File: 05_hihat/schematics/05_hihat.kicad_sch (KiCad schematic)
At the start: 69 parts, among them J1 Output, J2 Gate In, J3 Eurorack 10 pin, J4 Accent CV In, J5 Decay CV, Q1 BC548, Q2 BC548, Q4 BC558, Q5 BC558, U1 TL074, U2 40106

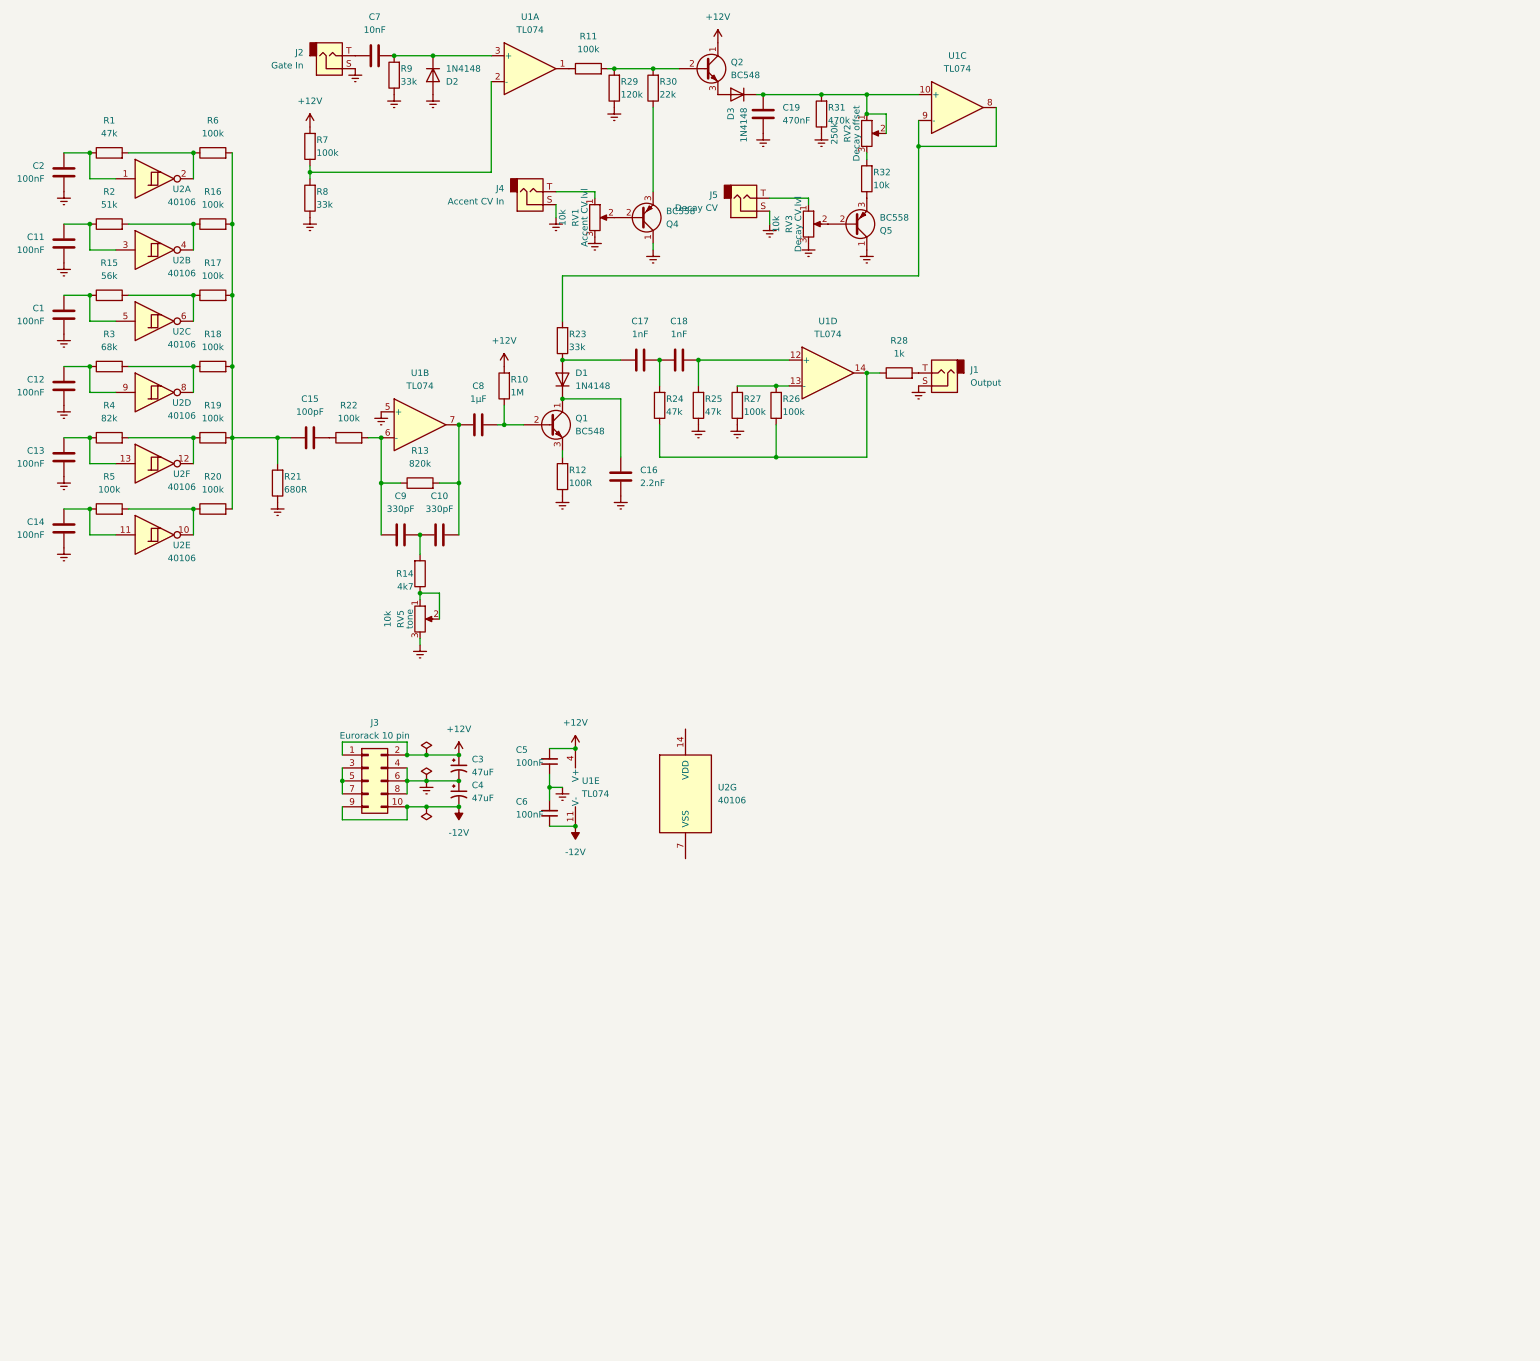
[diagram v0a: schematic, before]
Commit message: added stripboard for 05 hihat
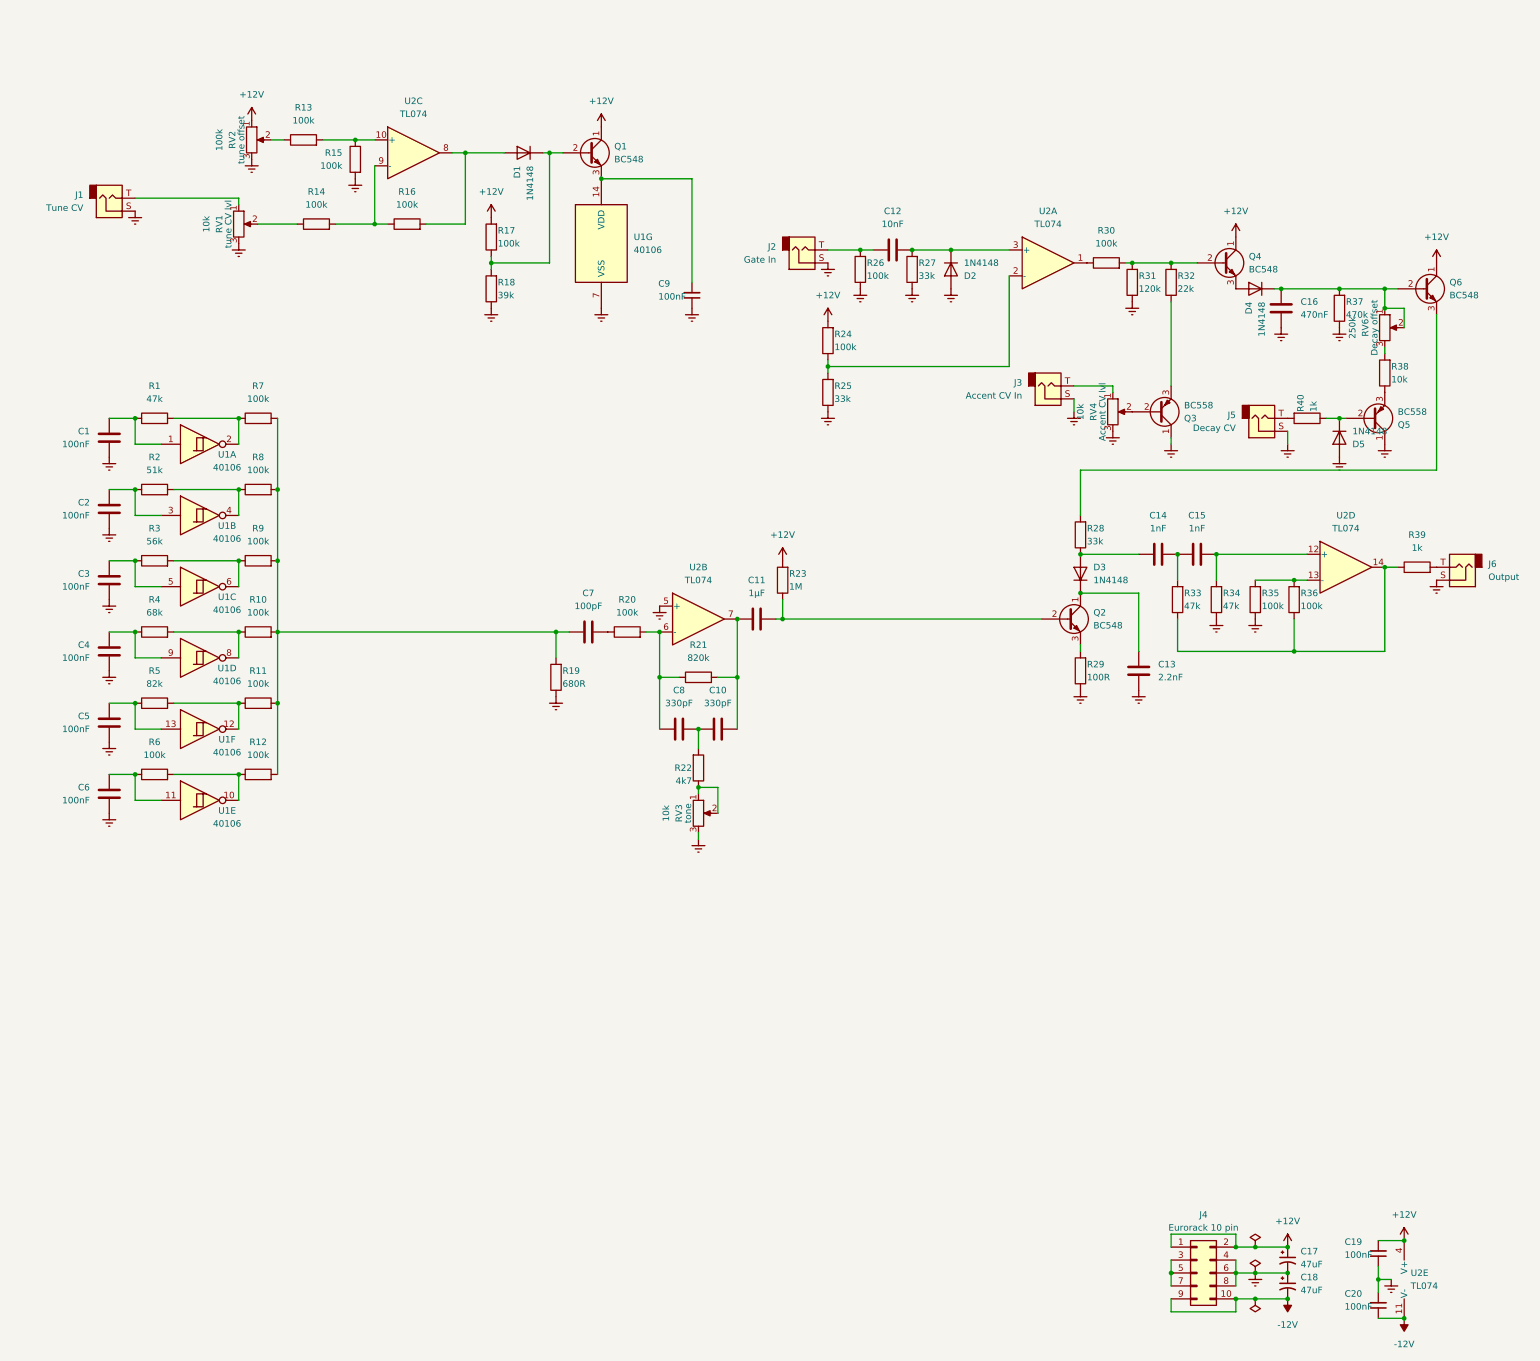
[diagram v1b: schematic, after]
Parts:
- removed C11, C12, C13, C14: 100nF, Capacitor_THT:C_Rect_L7.0mm_W2.5mm_P5.00mm, symbol Device:C
- removed R19, R20: 100k, Resistor_THT:R_Axial_DIN0207_L6.3mm_D2.5mm_P10.16mm_Horizontal, symbol Device:R
- removed RV3: 10k, Potentiometer_THT:Potentiometer_Alpha_RD901F-40-00D_Single_Vertical, symbol Device:R_Potentiometer
- removed unit 3 of U1
- removed unit 6 of U2
- removed unit 5 of U2
- removed unit 4 of U2
- removed unit 2 of U2
- removed unit 1 of U2
- removed unit 3 of U2
- added C3, C4, C5, C6: 100nF, Capacitor_THT:C_Rect_L7.0mm_W2.5mm_P5.00mm, symbol Device:C
- added C9: 100nF, Capacitor_THT:C_Disc_D6.0mm_W2.5mm_P5.00mm, symbol Device:C_Small
- added D1, D5: 1N4148, Diode_THT:D_T-1_P10.16mm_Horizontal, symbol Device:D
- added J1: Tune CV, Connector_Audio:Jack_6.35mm_Neutrik_NJ5FD-V_Vertical, symbol Connector:AudioJack2
- added Q1, Q6: BC548, Package_TO_SOT_THT:TO-92_Inline, symbol Transistor_BJT:BC548
- added R10, R11, R12, R13, R14, R26, R7, R8, R9: 100k, Resistor_THT:R_Axial_DIN0207_L6.3mm_D2.5mm_P10.16mm_Horizontal, symbol Device:R
- added R40: 1k, Resistor_THT:R_Axial_DIN0207_L6.3mm_D2.5mm_P10.16mm_Horizontal, symbol Device:R
- added RV1: 10k, Potentiometer_THT:Potentiometer_Alpha_RD901F-40-00D_Single_Vertical, symbol Device:R_Potentiometer
- added RV2: 100k, Potentiometer_THT:Potentiometer_Alpha_RD901F-40-00D_Single_Vertical, symbol Device:R_Potentiometer
- added unit 2 of U1
- added unit 4 of U1
- added unit 5 of U1
- added unit 1 of U1
- added unit 6 of U1
- added unit 3 of U1
- added unit 3 of U2
- R15: value 56k -> 100k
- R18: value 100k -> 39k
- R3: value 68k -> 56k
- R4: value 82k -> 68k
- R5: value 100k -> 82k
- renumbered C8 to C11, C7 to C12, C16 to C13, C17 to C14, C18 to C15, C19 to C16, C3 to C17, C4 to C18, C5 to C19, C6 to C20, C15 to C7, C9 to C8, D1 to D3, D3 to D4, J4 to J3, J3 to J4, J1 to J6, Q1 to Q2, Q4 to Q3, Q2 to Q4, R21 to R19, R22 to R20, R13 to R21, R14 to R22, R10 to R23, R7 to R24, R8 to R25, R9 to R27, R23 to R28, R12 to R29, R11 to R30, R29 to R31, R30 to R32, R24 to R33, R25 to R34, R27 to R35, R26 to R36, R31 to R37, R32 to R38, R28 to R39, RV5 to RV3, RV1 to RV4, RV2 to RV6, U2 to U1, U1 to U2
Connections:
- net +12V: now also R17.2, Q1.1 (C), Q6.1 (C), RV2.1
- net GNDREF: now also R15.2, R18.1, U1.7 (VSS), C3.2, C4.2, C5.2, C6.2, C9.1, D5.2 (A), J1.S, R26.1, RV1.3, RV2.3
- net at J5.T: now also R40.2
- net at R2.1: now also C2.1, U1.3
- net at R4.2: now also R10.1, U1.8
- net at R4.1: now also C4.1, U1.9
- net at U1.14 (VDD): now also C9.2, Q1.3 (E)
- net at R5.2: now also R11.1, U1.12
- net at R5.1: now also C5.1, U1.13
- net at C12.1, J2.T: now also R26.2
- net at Q5.2 (B): now also D5.1 (K), R40.1
- net at R3.1: now also C3.1, U1.5
- net at R3.2: now also R9.1, U1.6; no longer R18.1
- net at C16.1, D4.1 (K), R37.2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: now also Q6.2 (B)
- net at R1.1: now also C1.1, U1.1; no longer C2.1
- net at R2.2: now also R8.1, U1.4; no longer R16.1
- net at R15.1: now also R13.2, U2.10 (+); no longer C1.1
- net at R17.1: now also R18.2, D1.1 (K), Q1.2 (B); no longer R15.2
- net at R28.2: now also Q6.3 (E)
- net at R6.1: now also C6.1, U1.11; no longer R1.2
- new net: J1.T, RV1.1
- new net: R14.1, RV1.2
- new net: R14.2, R16.1, U2.9 (-)
- new net: D1.2 (A), R16.2, U2.8
- new net: C7.1, R10.2, R11.2, R12.2, R19.2, R7.2, R8.2, R9.2
- new net: R1.2, R7.1, U1.2
- new net: R12.1, R6.2, U1.10
- new net: R13.1, RV2.2
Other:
- moved on the sheet: C10, C11, C12, C13, C14, C15, C16, C17, C18, C19, C20, C7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

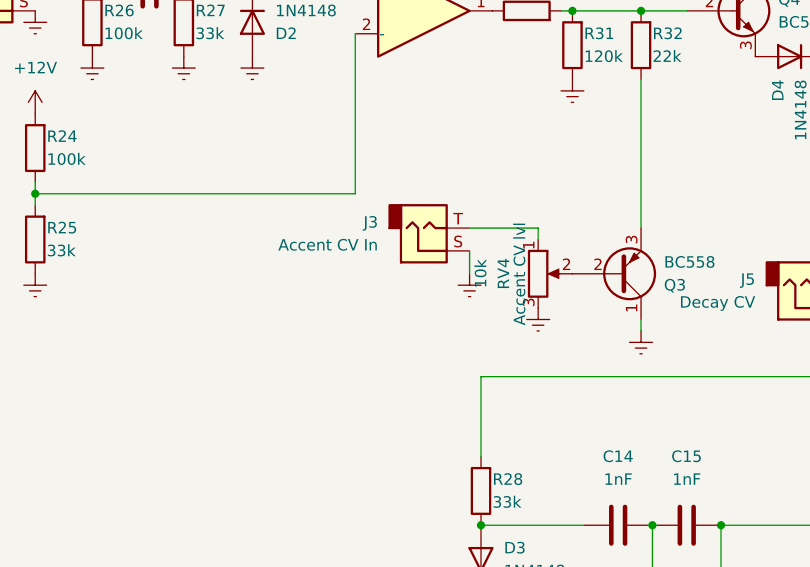
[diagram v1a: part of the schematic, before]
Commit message: fixed some values in the schematic
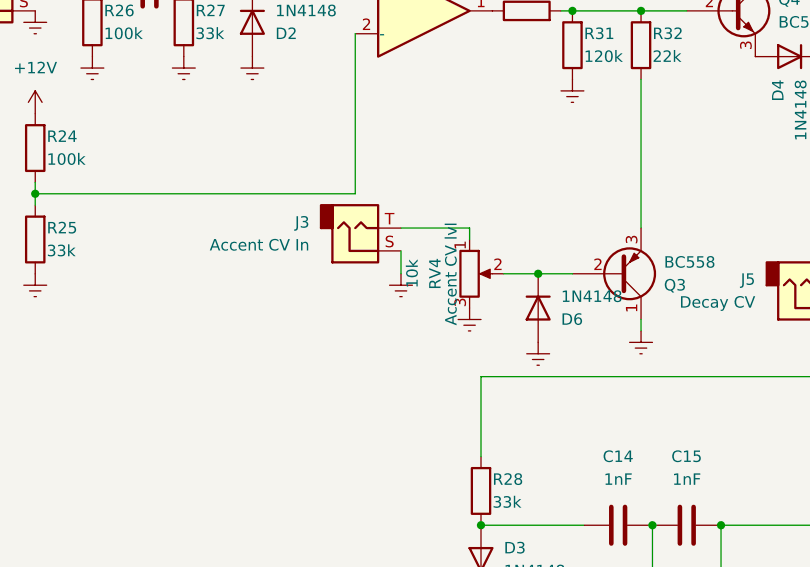
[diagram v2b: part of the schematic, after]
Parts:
- added D6: 1N4148, Diode_THT:D_T-1_P10.16mm_Horizontal, symbol Device:D
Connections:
- net GNDREF: now also D6.2 (A)
- net at Q3.2 (B), RV4.2: now also D6.1 (K)
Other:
- moved on the sheet: J3, RV4
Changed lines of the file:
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@@
 	)
 	(junction
+		(at 229.87 96.52)
+		(diameter 0)
+		(color 0 0 0 0)
+	)
+	(junction
 		(at 58.42 153.67)
 		(diameter 0)
@@
 	(wire
 		(pts
+			(xy 229.87 96.52) (xy 233.68 96.52)
+		)
+		(stroke
+			(width 0)
+			(type default)
+		)
+	)
+	(wire
+		(pts
 			(xy 223.52 116.84) (xy 223.52 107.95)
 		)
@@
 	(wire
 		(pts
+			(xy 226.06 96.52) (xy 229.87 96.52)
+		)
+		(stroke
+			(width 0)
+			(type default)
+		)
+	)
+	(wire
+		(pts
 			(xy 285.75 127) (xy 283.21 127)
 		)
@@
 	(wire
 		(pts
-			(xy 229.87 91.44) (xy 222.25 91.44)
+			(xy 222.25 91.44) (xy 214.63 91.44)
 		)
 		(stroke
@@
 	(wire
 		(pts
-			(xy 229.87 92.71) (xy 229.87 91.44)
+			(xy 222.25 92.71) (xy 222.25 91.44)
 		)
 		(stroke
@@
 	(wire
 		(pts
-			(xy 222.25 96.52) (xy 222.25 93.98)
+			(xy 214.63 96.52) (xy 214.63 93.98)
 		)
 		(stroke
@@
 	(symbol
 		(lib_id "power:GNDREF")
-		(at 222.25 96.52 0)
+		(at 214.63 96.52 0)
 		(unit 1)
 		(exclude_from_sim no)
@@
 		(fields_autoplaced yes)
 		(property "Reference" "#PWR027"
-			(at 222.25 102.87 0)
+			(at 214.63 102.87 0)
 			(effects
 				(font
@@
 		)
 		(property "Value" "GNDREF"
-			(at 222.25 101.6 0)
+			(at 214.63 101.6 0)
 			(effects
 				(font
@@
 		)
 		(property "Footprint" ""
-			(at 222.25 96.52 0)
+			(at 214.63 96.52 0)
 			(effects
 				(font
@@
 		)
 		(property "Datasheet" ""
-			(at 222.25 96.52 0)
+			(at 214.63 96.52 0)
 			(effects
 				(font
@@
 		)
 		(property "Description" ""
-			(at 222.25 96.52 0)
+			(at 214.63 96.52 0)
 			(effects
 				(font
@@
 	(symbol
 		(lib_id "Device:R_Potentiometer")
-		(at 229.87 96.52 0)
+		(at 222.25 96.52 0)
 		(unit 1)
 		(exclude_from_sim no)
@@
 		(dnp no)
 		(property "Reference" "RV4"
-			(at 226.06 96.52 90)
+			(at 218.44 96.52 90)
 			(effects
 				(font
@@
 		)
 		(property "Value" "10k"
-			(at 223.52 96.52 90)
+			(at 215.9 96.52 90)
 			(effects
 				(font
@@
 		)
 		(property "Footprint" "Potentiometer_THT:Potentiometer_Alpha_RD901F-40-00D_Single_Vertical"
-			(at 229.87 96.52 0)
+			(at 222.25 96.52 0)
 			(effects
 				(font
@@
 		)
 		(property "Datasheet" "~"
-			(at 229.87 96.52 0)
+			(at 222.25 96.52 0)
 			(effects
 				(font
@@
 		)
 		(property "Description" "Accent CV lvl"
-			(at 227.838 96.52 90)
+			(at 220.218 96.52 90)
 			(effects
 				(font
@@
 	)
 	(symbol
+		(lib_id "Device:D")
+		(at 229.87 100.33 90)
+		(mirror x)
+		(unit 1)
+		(exclude_from_sim no)
+		(in_bom yes)
+		(on_board yes)
+		(dnp no)
+		(property "Reference" "D6"
+			(at 232.41 101.6001 90)
+			(effects
+				(font
+					(size 1.27 1.27)
+				)
+				(justify right)
+			)
+		)
+		(property "Value" "1N4148"
+			(at 232.41 99.0601 90)
+			(effects
+				(font
+					(size 1.27 1.27)
+				)
+				(justify right)
+			)
+		)
+		(property "Footprint" "Diode_THT:D_T-1_P10.16mm_Horizontal"
+			(at 229.87 100.33 0)
+			(effects
+				(font
+					(size 1.27 1.27)
+				)
+				(hide yes)
+			)
+		)
+		(property "Datasheet" "~"
+			(at 229.87 100.33 0)
+			(effects
+				(font
+					(size 1.27 1.27)
+				)
+				(hide yes)
+			)
+		)
+		(property "Description" ""
+			(at 229.87 100.33 0)
+			(effects
+				(font
+					(size 1.27 1.27)
+				)
+				(hide yes)
+			)
+		)
+		(pin "1"
+		)
+		(pin "2"
+		)
+		(instances
+			(project "05_hihat"
+				(path "/2375ec83-956c-4ce3-8106-f4a8f815549e"
+					(reference "D6")
+					(unit 1)
+				)
+			)
+		)
+	)
+	(symbol
 		(lib_id "Device:C")
 		(at 186.69 64.77 90)
@@
 	(symbol
 		(lib_id "Connector:AudioJack2")
-		(at 217.17 91.44 0)
+		(at 209.55 91.44 0)
 		(mirror x)
 		(unit 1)
@@
 		(dnp no)
 		(property "Reference" "J3"
-			(at 212.09 90.8049 0)
+			(at 204.47 90.8049 0)
 			(effects
 				(font
@@
 		)
 		(property "Value" "Accent CV In"
-			(at 212.09 93.3449 0)
+			(at 204.47 93.3449 0)
 			(effects
 				(font
@@
 		)
 		(property "Footprint" "Connector_Audio:Jack_6.35mm_Neutrik_NJ5FD-V_Vertical"
-			(at 217.17 91.44 0)
+			(at 209.55 91.44 0)
 			(effects
 				(font
@@
 		)
 		(property "Datasheet" "~"
-			(at 217.17 91.44 0)
+			(at 209.55 91.44 0)
 			(effects
 				(font
@@
 		)
 		(property "Description" ""
-			(at 217.17 91.44 0)
+			(at 209.55 91.44 0)
 			(effects
 				(font
@@
 	(symbol
 		(lib_id "power:GNDREF")
+		(at 229.87 104.14 0)
+		(unit 1)
+		(exclude_from_sim no)
+		(in_bom yes)
+		(on_board yes)
+		(dnp no)
+		(fields_autoplaced yes)
+		(property "Reference" "#PWR049"
+			(at 229.87 110.49 0)
+			(effects
+				(font
+					(size 1.27 1.27)
+				)
+				(hide yes)
+			)
+		)
+		(property "Value" "GNDREF"
+			(at 229.87 109.22 0)
+			(effects
+				(font
+					(size 1.27 1.27)
+				)
+				(hide yes)
+			)
+		)
+		(property "Footprint" ""
+			(at 229.87 104.14 0)
+			(effects
+				(font
+					(size 1.27 1.27)
+				)
+				(hide yes)
+			)
+		)
+		(property "Datasheet" ""
+			(at 229.87 104.14 0)
+			(effects
+				(font
+					(size 1.27 1.27)
+				)
+				(hide yes)
+			)
+		)
+		(property "Description" ""
+			(at 229.87 104.14 0)
+			(effects
+				(font
+					(size 1.27 1.27)
+				)
+				(hide yes)
+			)
+		)
+		(pin "1"
+		)
+		(instances
+			(project "05_hihat"
+				(path "/2375ec83-956c-4ce3-8106-f4a8f815549e"
+					(reference "#PWR049")
+					(unit 1)
+				)
+			)
+		)
+	)
+	(symbol
+		(lib_id "power:GNDREF")
 		(at 223.52 151.13 0)
 		(unit 1)
@@
 	(symbol
 		(lib_id "power:GNDREF")
-		(at 229.87 100.33 0)
+		(at 222.25 100.33 0)
 		(unit 1)
 		(exclude_from_sim no)
@@
 		(fields_autoplaced yes)
 		(property "Reference" "#PWR029"
-			(at 229.87 106.68 0)
+			(at 222.25 106.68 0)
 			(effects
 				(font
@@
 		)
 		(property "Value" "GNDREF"
-			(at 229.87 105.41 0)
+			(at 222.25 105.41 0)
 			(effects
 				(font
@@
 		)
 		(property "Footprint" ""
-			(at 229.87 100.33 0)
+			(at 222.25 100.33 0)
 			(effects
 				(font
@@
 		)
 		(property "Datasheet" ""
-			(at 229.87 100.33 0)
+			(at 222.25 100.33 0)
 			(effects
 				(font
@@
 		)
 		(property "Description" ""
-			(at 229.87 100.33 0)
+			(at 222.25 100.33 0)
 			(effects
 				(font
